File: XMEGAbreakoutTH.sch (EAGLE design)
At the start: 23 parts, among them IC1 XMEGA16A4

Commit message: latest
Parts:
- added JP6: (no value), fab:PINHD-2X3-SMD
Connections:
- new net DAT: IC1.PDI_DATA, JP6.1
- net GND: now also JP6.6
- net RESET: now also JP6.5; no longer JP4.5
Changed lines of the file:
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@@
 <grid distance="0.1" unitdist="inch" unit="inch" style="lines" multiple="1" display="no" altdistance="0.01" altunitdist="inch" altunit="inch"/>
 <layers>
-<layer number="1" name="Top" color="4" fill="1" visible="no" active="no"/>
-<layer number="2" name="Route2" color="1" fill="3" visible="no" active="no"/>
-<layer number="3" name="Route3" color="4" fill="3" visible="no" active="no"/>
-<layer number="14" name="Route14" color="1" fill="6" visible="no" active="no"/>
-<layer number="15" name="Route15" color="4" fill="6" visible="no" active="no"/>
-<layer number="16" name="Bottom" color="1" fill="1" visible="no" active="no"/>
-<layer number="17" name="Pads" color="2" fill="1" visible="no" active="no"/>
-<layer number="18" name="Vias" color="2" fill="1" visible="no" active="no"/>
-<layer number="19" name="Unrouted" color="6" fill="1" visible="no" active="no"/>
-<layer number="20" name="Dimension" color="15" fill="1" visible="no" active="no"/>
-<layer number="21" name="tPlace" color="7" fill="1" visible="no" active="no"/>
-<layer number="22" name="bPlace" color="7" fill="1" visible="no" active="no"/>
-<layer number="23" name="tOrigins" color="15" fill="1" visible="no" active="no"/>
-<layer number="24" name="bOrigins" color="15" fill="1" visible="no" active="no"/>
-<layer number="25" name="tNames" color="7" fill="1" visible="no" active="no"/>
-<layer number="26" name="bNames" color="7" fill="1" visible="no" active="no"/>
-<layer number="27" name="tValues" color="7" fill="1" visible="no" active="no"/>
-<layer number="28" name="bValues" color="7" fill="1" visible="no" active="no"/>
+<layer number="1" name="Top" color="4" fill="1" visible="yes" active="no"/>
+<layer number="2" name="Route2" color="1" fill="3" visible="yes" active="no"/>
+<layer number="3" name="Route3" color="4" fill="3" visible="yes" active="no"/>
+<layer number="14" name="Route14" color="1" fill="6" visible="yes" active="no"/>
+<layer number="15" name="Route15" color="4" fill="6" visible="yes" active="no"/>
+<layer number="16" name="Bottom" color="1" fill="1" visible="yes" active="no"/>
+<layer number="17" name="Pads" color="2" fill="1" visible="yes" active="no"/>
+<layer number="18" name="Vias" color="2" fill="1" visible="yes" active="no"/>
+<layer number="19" name="Unrouted" color="6" fill="1" visible="yes" active="no"/>
+<layer number="20" name="Dimension" color="15" fill="1" visible="yes" active="no"/>
+<layer number="21" name="tPlace" color="7" fill="1" visible="yes" active="no"/>
+<layer number="22" name="bPlace" color="7" fill="1" visible="yes" active="no"/>
+<layer number="23" name="tOrigins" color="15" fill="1" visible="yes" active="no"/>
+<layer number="24" name="bOrigins" color="15" fill="1" visible="yes" active="no"/>
+<layer number="25" name="tNames" color="7" fill="1" visible="yes" active="no"/>
+<layer number="26" name="bNames" color="7" fill="1" visible="yes" active="no"/>
+<layer number="27" name="tValues" color="7" fill="1" visible="yes" active="no"/>
+<layer number="28" name="bValues" color="7" fill="1" visible="yes" active="no"/>
 <layer number="29" name="tStop" color="7" fill="3" visible="no" active="no"/>
 <layer number="30" name="bStop" color="7" fill="6" visible="no" active="no"/>
@@
 <layer number="35" name="tGlue" color="7" fill="4" visible="no" active="no"/>
 <layer number="36" name="bGlue" color="7" fill="5" visible="no" active="no"/>
-<layer number="37" name="tTest" color="7" fill="1" visible="no" active="no"/>
-<layer number="38" name="bTest" color="7" fill="1" visible="no" active="no"/>
+<layer number="37" name="tTest" color="7" fill="1" visible="yes" active="no"/>
+<layer number="38" name="bTest" color="7" fill="1" visible="yes" active="no"/>
 <layer number="39" name="tKeepout" color="4" fill="11" visible="no" active="no"/>
 <layer number="40" name="bKeepout" color="1" fill="11" visible="no" active="no"/>
@@
 <layer number="44" name="Drills" color="7" fill="1" visible="no" active="no"/>
 <layer number="45" name="Holes" color="7" fill="1" visible="no" active="no"/>
-<layer number="46" name="Milling" color="3" fill="1" visible="no" active="no"/>
-<layer number="47" name="Measures" color="7" fill="1" visible="no" active="no"/>
-<layer number="48" name="Document" color="7" fill="1" visible="no" active="no"/>
-<layer number="49" name="Reference" color="7" fill="1" visible="no" active="no"/>
-<layer number="50" name="dxf" color="7" fill="1" visible="no" active="no"/>
-<layer number="51" name="tDocu" color="7" fill="1" visible="no" active="no"/>
-<layer number="52" name="bDocu" color="7" fill="1" visible="no" active="no"/>
-<layer number="53" name="tGND_GNDA" color="7" fill="9" visible="no" active="no"/>
-<layer number="54" name="bGND_GNDA" color="1" fill="9" visible="no" active="no"/>
-<layer number="56" name="wert" color="7" fill="1" visible="no" active="no"/>
+<layer number="46" name="Milling" color="3" fill="1" visible="yes" active="no"/>
+<layer number="47" name="Measures" color="7" fill="1" visible="yes" active="no"/>
+<layer number="48" name="Document" color="7" fill="1" visible="yes" active="no"/>
+<layer number="49" name="Reference" color="7" fill="1" visible="yes" active="no"/>
+<layer number="50" name="dxf" color="7" fill="1" visible="yes" active="no"/>
+<layer number="51" name="tDocu" color="7" fill="1" visible="yes" active="no"/>
+<layer number="52" name="bDocu" color="7" fill="1" visible="yes" active="no"/>
+<layer number="53" name="tGND_GNDA" color="7" fill="9" visible="yes" active="no"/>
+<layer number="54" name="bGND_GNDA" color="1" fill="9" visible="yes" active="no"/>
+<layer number="56" name="wert" color="7" fill="1" visible="yes" active="no"/>
 <layer number="90" name="Modules" color="5" fill="1" visible="yes" active="yes"/>
 <layer number="91" name="Nets" color="2" fill="1" visible="yes" active="yes"/>
@@
 <part name="JP8" library="SparkFun" deviceset="M02" device="PTH"/>
 <part name="JP9" library="SparkFun" deviceset="M02" device="PTH"/>
+<part name="JP6" library="fab" deviceset="PINHD-2X3-SMD" device=""/>
+<part name="GND6" library="SparkFun" deviceset="GND" device=""/>
 </parts>
 <sheets>
@@
 <instance part="JP8" gate="G$1" x="137.16" y="160.02"/>
 <instance part="JP9" gate="G$1" x="137.16" y="144.78"/>
+<instance part="JP6" gate="A" x="139.7" y="20.32"/>
+<instance part="GND6" gate="1" x="157.48" y="12.7"/>
 </instances>
 <busses>
@@
 </segment>
 <segment>
-<pinref part="JP4" gate="A" pin="5"/>
-<wire x1="137.16" y1="45.72" x2="121.92" y2="45.72" width="0.1524" layer="91"/>
-<label x="121.92" y="45.72" size="1.778" layer="95"/>
+<pinref part="JP6" gate="A" pin="5"/>
+<wire x1="137.16" y1="17.78" x2="121.92" y2="17.78" width="0.1524" layer="91"/>
+<label x="121.92" y="17.78" size="1.778" layer="95"/>
 </segment>
 </net>
@@
 <label x="144.78" y="144.78" size="1.778" layer="95"/>
 </segment>
+<segment>
+<pinref part="JP6" gate="A" pin="6"/>
+<wire x1="144.78" y1="17.78" x2="157.48" y2="17.78" width="0.1524" layer="91"/>
+<pinref part="GND6" gate="1" pin="GND"/>
+<wire x1="157.48" y1="17.78" x2="157.48" y2="15.24" width="0.1524" layer="91"/>
+</segment>
 </net>
 <net name="VCC" class="0">
@@
 </segment>
 </net>
+<net name="DAT" class="0">
+<segment>
+<pinref part="JP6" gate="A" pin="1"/>
+<wire x1="137.16" y1="22.86" x2="121.92" y2="22.86" width="0.1524" layer="91"/>
+<label x="121.92" y="22.86" size="1.778" layer="95"/>
+</segment>
+<segment>
+<pinref part="IC1" gate="G$1" pin="PDI_DATA"/>
+<wire x1="20.32" y1="78.74" x2="7.62" y2="78.74" width="0.1524" layer="91"/>
+<label x="7.62" y="78.74" size="1.778" layer="95"/>
+</segment>
+</net>

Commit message: final pngs
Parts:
- removed C3: 0.1uF, fab:CAP-US1206
- removed JUMPER1, JUMPER2: 0, fab:RES-US1206FAB
- added JUMPER: 0Ohm, fab:RES-US1206FAB
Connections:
- net D+: now also IC1.PD7, JP3.1, U$2.Y; no longer IC1.PD6, JP3.2, U$2.GND
- net D-: now also IC1.PD6, JP3.2, U$2.GND; no longer IC1.PD7, JP3.1, U$2.Y
- net GND: no longer C3.2
- net RESET: no longer C3.1
- net VCC: now also JP6.2
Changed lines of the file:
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@@
 <?xml version="1.0" encoding="utf-8"?>
 <!DOCTYPE eagle SYSTEM "eagle.dtd">
-<eagle version="7.1.0">
+<eagle version="7.5.0">
 <drawing>
 <settings>
@@
 <part name="R1" library="fab" deviceset="RES-US" device="1206FAB" value="10K"/>
 <part name="S1" library="fab" deviceset="6MM_SWITCH" device="6MM_SWITCH"/>
-<part name="C3" library="fab" deviceset="CAP-US" device="1206" value="0.1uF"/>
 <part name="U$1" library="fab" deviceset="USB_MINIB" device=""/>
 <part name="JP4" library="fab" deviceset="PINHD-2X3-SMD" device=""/>
@@
 <part name="P+4" library="SparkFun" deviceset="VCC" device=""/>
 <part name="GND5" library="SparkFun" deviceset="GND" device=""/>
-<part name="JUMPER1" library="fab" deviceset="RES-US" device="1206FAB" value="0"/>
-<part name="JUMPER2" library="fab" deviceset="RES-US" device="1206FAB" value="0"/>
 <part name="C5" library="fab" deviceset="CAP-US" device="1206" value="4.7uF"/>
 <part name="U$2" library="SparkFun" deviceset="INVERTER" device=""/>
@@
 <part name="JP6" library="fab" deviceset="PINHD-2X3-SMD" device=""/>
 <part name="GND6" library="SparkFun" deviceset="GND" device=""/>
+<part name="P+2" library="SparkFun" deviceset="VCC" device=""/>
+<part name="JUMPER" library="fab" deviceset="RES-US" device="1206FAB" value="0Ohm"/>
 </parts>
 <sheets>
@@
 <instance part="R1" gate="G$1" x="-25.4" y="93.98" rot="R180"/>
 <instance part="S1" gate="2" x="-48.26" y="93.98" rot="R270"/>
-<instance part="C3" gate="G$1" x="-48.26" y="76.2" rot="R180"/>
 <instance part="U$1" gate="G$1" x="-63.5" y="154.94" rot="R180"/>
 <instance part="JP4" gate="A" x="139.7" y="48.26"/>
@@
 <instance part="P+4" gate="1" x="104.14" y="175.26"/>
 <instance part="GND5" gate="1" x="106.68" y="142.24"/>
-<instance part="JUMPER1" gate="G$1" x="0" y="175.26"/>
-<instance part="JUMPER2" gate="G$1" x="0" y="167.64"/>
 <instance part="C5" gate="G$1" x="30.48" y="162.56" rot="R270"/>
 <instance part="U$2" gate="G$1" x="30.48" y="116.84"/>
@@
 <instance part="JP6" gate="A" x="139.7" y="20.32"/>
 <instance part="GND6" gate="1" x="157.48" y="12.7"/>
+<instance part="P+2" gate="1" x="157.48" y="25.4"/>
+<instance part="JUMPER" gate="G$1" x="88.9" y="114.3"/>
 </instances>
 <busses>
@@
 <wire x1="-43.18" y1="93.98" x2="-43.18" y2="91.44" width="0.1524" layer="91"/>
 <junction x="-43.18" y="93.98"/>
-<pinref part="C3" gate="G$1" pin="1"/>
-<wire x1="-45.72" y1="76.2" x2="-35.56" y2="76.2" width="0.1524" layer="91"/>
-<wire x1="-35.56" y1="76.2" x2="-35.56" y2="93.98" width="0.1524" layer="91"/>
 <junction x="-35.56" y="93.98"/>
 <wire x1="-35.56" y1="93.98" x2="-35.56" y2="106.68" width="0.1524" layer="91"/>
@@
 <net name="D+" class="0">
 <segment>
-<pinref part="IC1" gate="G$1" pin="PD6"/>
-<pinref part="JP3" gate="G$1" pin="2"/>
-<wire x1="73.66" y1="22.86" x2="83.82" y2="22.86" width="0.1524" layer="91"/>
-<label x="76.2" y="22.86" size="1.778" layer="95"/>
-</segment>
-<segment>
 <pinref part="U$1" gate="G$1" pin="D+"/>
 <wire x1="-60.96" y1="152.4" x2="-55.88" y2="152.4" width="0.1524" layer="91"/>
@@
 </segment>
 <segment>
-<pinref part="U$2" gate="G$1" pin="GND"/>
-<wire x1="20.32" y1="111.76" x2="7.62" y2="111.76" width="0.1524" layer="91"/>
-<label x="7.62" y="111.76" size="1.778" layer="95"/>
+<pinref part="IC1" gate="G$1" pin="PD7"/>
+<pinref part="JP3" gate="G$1" pin="1"/>
+<wire x1="73.66" y1="25.4" x2="83.82" y2="25.4" width="0.1524" layer="91"/>
+<label x="76.2" y="25.4" size="1.778" layer="95"/>
+</segment>
+<segment>
+<pinref part="U$2" gate="G$1" pin="Y"/>
+<wire x1="40.64" y1="111.76" x2="50.8" y2="111.76" width="0.1524" layer="91"/>
+<label x="45.72" y="111.76" size="1.778" layer="95"/>
 </segment>
 </net>
@@
 <pinref part="S1" gate="2" pin="P1"/>
 <wire x1="-53.34" y1="93.98" x2="-53.34" y2="91.44" width="0.1524" layer="91"/>
-<wire x1="-53.34" y1="93.98" x2="-60.96" y2="93.98" width="0.1524" layer="91"/>
 <junction x="-53.34" y="93.98"/>
-<pinref part="C3" gate="G$1" pin="2"/>
-<wire x1="-53.34" y1="76.2" x2="-60.96" y2="76.2" width="0.1524" layer="91"/>
-<wire x1="-60.96" y1="76.2" x2="-60.96" y2="93.98" width="0.1524" layer="91"/>
 <pinref part="GND4" gate="1" pin="GND"/>
-<wire x1="-60.96" y1="93.98" x2="-73.66" y2="93.98" width="0.1524" layer="91"/>
+<wire x1="-53.34" y1="93.98" x2="-73.66" y2="93.98" width="0.1524" layer="91"/>
 <wire x1="-73.66" y1="93.98" x2="-73.66" y2="91.44" width="0.1524" layer="91"/>
-<junction x="-60.96" y="93.98"/>
 </segment>
 <segment>
@@
 <label x="144.78" y="162.56" size="1.778" layer="95"/>
 </segment>
+<segment>
+<pinref part="JP6" gate="A" pin="2"/>
+<wire x1="144.78" y1="22.86" x2="157.48" y2="22.86" width="0.1524" layer="91"/>
+<pinref part="P+2" gate="1" pin="VCC"/>
+<wire x1="157.48" y1="25.4" x2="157.48" y2="22.86" width="0.1524" layer="91"/>
+</segment>
 </net>
 <net name="D-" class="0">
@@
 </segment>
 <segment>
-<pinref part="IC1" gate="G$1" pin="PD7"/>
-<pinref part="JP3" gate="G$1" pin="1"/>
-<wire x1="73.66" y1="25.4" x2="83.82" y2="25.4" width="0.1524" layer="91"/>
-<label x="76.2" y="25.4" size="1.778" layer="95"/>
-</segment>
-<segment>
-<pinref part="U$2" gate="G$1" pin="Y"/>
-<wire x1="40.64" y1="111.76" x2="50.8" y2="111.76" width="0.1524" layer="91"/>
-<label x="45.72" y="111.76" size="1.778" layer="95"/>
-</segment>
-</net>
+<pinref part="IC1" gate="G$1" pin="PD6"/>
+<pinref part="JP3" gate="G$1" pin="2"/>
+<wire x1="73.66" y1="22.86" x2="83.82" y2="22.86" width="0.1524" layer="91"/>
+<label x="76.2" y="22.86" size="1.778" layer="95"/>
+</segment>
+<segment>
+<pinref part="U$2" gate="G$1" pin="GND"/>
+<wire x1="20.32" y1="111.76" x2="7.62" y2="111.76" width="0.1524" layer="91"/>
+<label x="7.62" y="111.76" size="1.778" layer="95"/>
+</segment>
+</net>

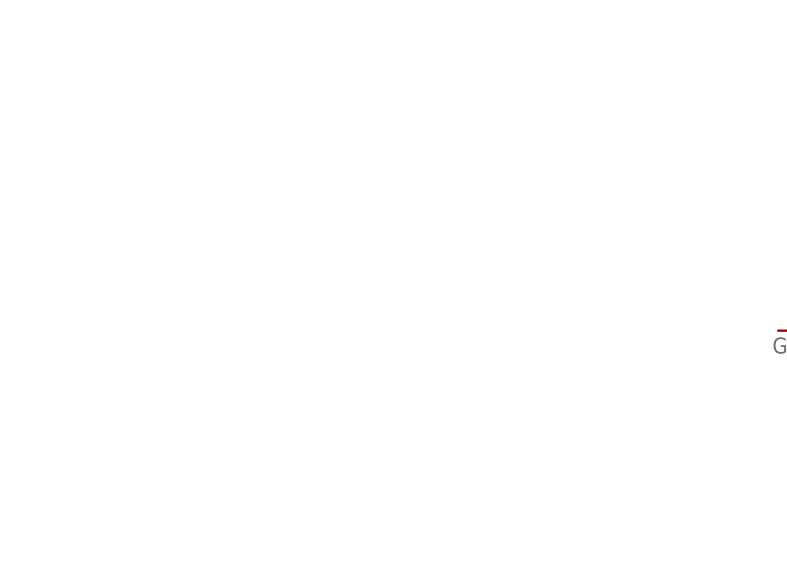
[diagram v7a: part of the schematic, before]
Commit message: solder jumper on 5V
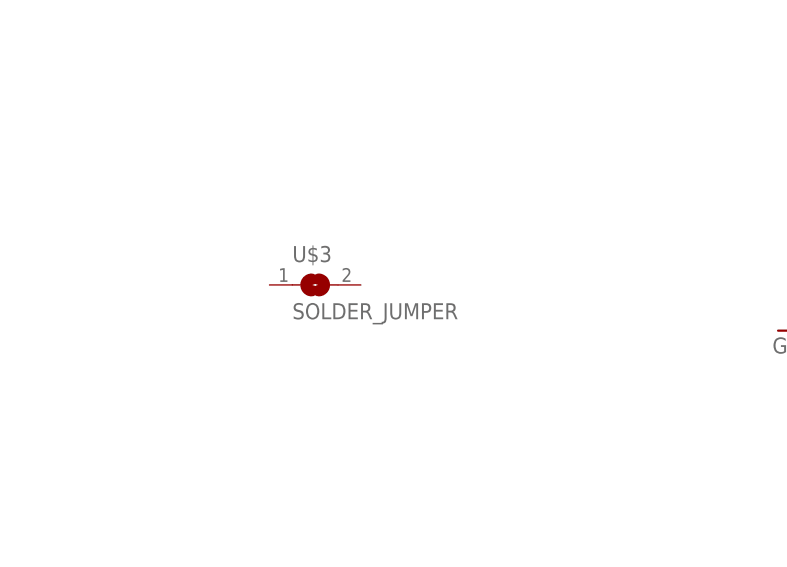
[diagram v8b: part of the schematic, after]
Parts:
- added U$3: SOLDER_JUMPER, fab:SOLDER_JUMPER
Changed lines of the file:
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@@
 <grid distance="0.1" unitdist="inch" unit="inch" style="lines" multiple="1" display="no" altdistance="0.01" altunitdist="inch" altunit="inch"/>
 <layers>
-<layer number="1" name="Top" color="4" fill="1" visible="yes" active="no"/>
-<layer number="2" name="Route2" color="1" fill="3" visible="yes" active="no"/>
-<layer number="3" name="Route3" color="4" fill="3" visible="yes" active="no"/>
-<layer number="14" name="Route14" color="1" fill="6" visible="yes" active="no"/>
-<layer number="15" name="Route15" color="4" fill="6" visible="yes" active="no"/>
-<layer number="16" name="Bottom" color="1" fill="1" visible="yes" active="no"/>
-<layer number="17" name="Pads" color="2" fill="1" visible="yes" active="no"/>
-<layer number="18" name="Vias" color="2" fill="1" visible="yes" active="no"/>
-<layer number="19" name="Unrouted" color="6" fill="1" visible="yes" active="no"/>
-<layer number="20" name="Dimension" color="15" fill="1" visible="yes" active="no"/>
-<layer number="21" name="tPlace" color="7" fill="1" visible="yes" active="no"/>
-<layer number="22" name="bPlace" color="7" fill="1" visible="yes" active="no"/>
-<layer number="23" name="tOrigins" color="15" fill="1" visible="yes" active="no"/>
-<layer number="24" name="bOrigins" color="15" fill="1" visible="yes" active="no"/>
-<layer number="25" name="tNames" color="7" fill="1" visible="yes" active="no"/>
-<layer number="26" name="bNames" color="7" fill="1" visible="yes" active="no"/>
-<layer number="27" name="tValues" color="7" fill="1" visible="yes" active="no"/>
-<layer number="28" name="bValues" color="7" fill="1" visible="yes" active="no"/>
+<layer number="1" name="Top" color="4" fill="1" visible="no" active="no"/>
+<layer number="2" name="Route2" color="1" fill="3" visible="no" active="no"/>
+<layer number="3" name="Route3" color="4" fill="3" visible="no" active="no"/>
+<layer number="14" name="Route14" color="1" fill="6" visible="no" active="no"/>
+<layer number="15" name="Route15" color="4" fill="6" visible="no" active="no"/>
+<layer number="16" name="Bottom" color="1" fill="1" visible="no" active="no"/>
+<layer number="17" name="Pads" color="2" fill="1" visible="no" active="no"/>
+<layer number="18" name="Vias" color="2" fill="1" visible="no" active="no"/>
+<layer number="19" name="Unrouted" color="6" fill="1" visible="no" active="no"/>
+<layer number="20" name="Dimension" color="15" fill="1" visible="no" active="no"/>
+<layer number="21" name="tPlace" color="7" fill="1" visible="no" active="no"/>
+<layer number="22" name="bPlace" color="7" fill="1" visible="no" active="no"/>
+<layer number="23" name="tOrigins" color="15" fill="1" visible="no" active="no"/>
+<layer number="24" name="bOrigins" color="15" fill="1" visible="no" active="no"/>
+<layer number="25" name="tNames" color="7" fill="1" visible="no" active="no"/>
+<layer number="26" name="bNames" color="7" fill="1" visible="no" active="no"/>
+<layer number="27" name="tValues" color="7" fill="1" visible="no" active="no"/>
+<layer number="28" name="bValues" color="7" fill="1" visible="no" active="no"/>
 <layer number="29" name="tStop" color="7" fill="3" visible="no" active="no"/>
 <layer number="30" name="bStop" color="7" fill="6" visible="no" active="no"/>
@@
 <layer number="35" name="tGlue" color="7" fill="4" visible="no" active="no"/>
 <layer number="36" name="bGlue" color="7" fill="5" visible="no" active="no"/>
-<layer number="37" name="tTest" color="7" fill="1" visible="yes" active="no"/>
-<layer number="38" name="bTest" color="7" fill="1" visible="yes" active="no"/>
+<layer number="37" name="tTest" color="7" fill="1" visible="no" active="no"/>
+<layer number="38" name="bTest" color="7" fill="1" visible="no" active="no"/>
 <layer number="39" name="tKeepout" color="4" fill="11" visible="no" active="no"/>
 <layer number="40" name="bKeepout" color="1" fill="11" visible="no" active="no"/>
@@
 <layer number="44" name="Drills" color="7" fill="1" visible="no" active="no"/>
 <layer number="45" name="Holes" color="7" fill="1" visible="no" active="no"/>
-<layer number="46" name="Milling" color="3" fill="1" visible="yes" active="no"/>
-<layer number="47" name="Measures" color="7" fill="1" visible="yes" active="no"/>
-<layer number="48" name="Document" color="7" fill="1" visible="yes" active="no"/>
-<layer number="49" name="Reference" color="7" fill="1" visible="yes" active="no"/>
-<layer number="50" name="dxf" color="7" fill="1" visible="yes" active="no"/>
-<layer number="51" name="tDocu" color="7" fill="1" visible="yes" active="no"/>
-<layer number="52" name="bDocu" color="7" fill="1" visible="yes" active="no"/>
-<layer number="53" name="tGND_GNDA" color="7" fill="9" visible="yes" active="no"/>
-<layer number="54" name="bGND_GNDA" color="1" fill="9" visible="yes" active="no"/>
-<layer number="56" name="wert" color="7" fill="1" visible="yes" active="no"/>
+<layer number="46" name="Milling" color="3" fill="1" visible="no" active="no"/>
+<layer number="47" name="Measures" color="7" fill="1" visible="no" active="no"/>
+<layer number="48" name="Document" color="7" fill="1" visible="no" active="no"/>
+<layer number="49" name="Reference" color="7" fill="1" visible="no" active="no"/>
+<layer number="50" name="dxf" color="7" fill="1" visible="no" active="no"/>
+<layer number="51" name="tDocu" color="7" fill="1" visible="no" active="no"/>
+<layer number="52" name="bDocu" color="7" fill="1" visible="no" active="no"/>
+<layer number="53" name="tGND_GNDA" color="7" fill="9" visible="no" active="no"/>
+<layer number="54" name="bGND_GNDA" color="1" fill="9" visible="no" active="no"/>
+<layer number="56" name="wert" color="7" fill="1" visible="no" active="no"/>
 <layer number="90" name="Modules" color="5" fill="1" visible="yes" active="yes"/>
 <layer number="91" name="Nets" color="2" fill="1" visible="yes" active="yes"/>
@@
 <part name="P+2" library="SparkFun" deviceset="VCC" device=""/>
 <part name="JUMPER" library="fab" deviceset="RES-US" device="1206FAB" value="0Ohm"/>
+<part name="U$3" library="fab" deviceset="SOLDER_JUMPER" device=""/>
 </parts>
 <sheets>
@@
 <instance part="P+2" gate="1" x="157.48" y="25.4"/>
 <instance part="JUMPER" gate="G$1" x="88.9" y="114.3"/>
+<instance part="U$3" gate="G$1" x="-43.18" y="43.18"/>
 </instances>
 <busses>
